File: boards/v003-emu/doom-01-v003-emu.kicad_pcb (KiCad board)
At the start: 2 copper layers, 96 x 50 mm, 36 parts, among them SW9 JS102011SAQN, U1 CH32V003F4P6, U2 APS6404L-3SQR-SN, U3 W25Q128JVSIQ, U4 TPS61023DRLR

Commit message: PCBKit's mark and pcbkit.io on every board; the RP2350 handheld ready to order
The handheld runs from two 18650 cells in parallel behind a DW01A protector and a reverse-cell
P-MOSFET, charged at up to 500 mA from the Pico's USB-C by a BQ24075 (power path into VSYS, timers
off for 6 Ah), with an on/off switch on 3V3_EN, M3 holes, ground pours and the console on pads.
Every assembled part has a JLCPCB code in stock (Basic where there is one); the module sockets are
in the BOM, the modules listed in the order's README. Check complete, the ready review clean.
Every board: routed and checked complete with the new mark.
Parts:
- added logo: , Logo_PCBKit_pcbkit.io, F.Cu at (122.0, 192.2)
- SW1, SW2, SW3, SW4, SW5, SW6, SW7, SW8: value (none) -> TS-1187A-B-A-B

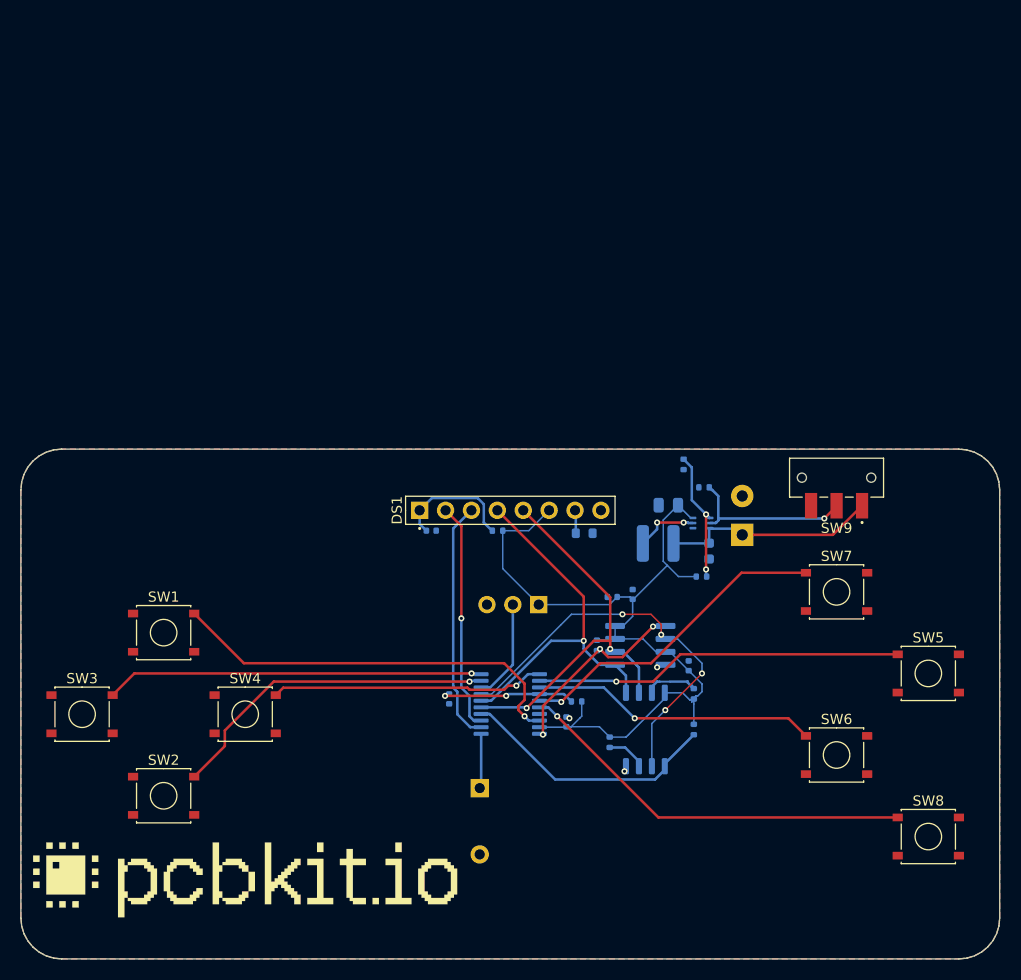
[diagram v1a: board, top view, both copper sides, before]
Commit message: v003-emu: two 18650 cells with protection, USB-C charging and an LDO; every part orderable
Two AA cells and a TPS61023 boost become two 18650 in parallel (Keystone 1042 holders on the
back) behind a reverse-cell P-FET and DW01A + FS8205A protection, a BQ24075 charger with power
path from a power-only USB-C port (750 mA PTC, TVS), and an AP2112K-3.3 LDO from SYS switched by
its enable (a boost cannot make 3.3 V from a cell above it). WCH-LinkE header J2 at the edge
(the ready lens now knows single-wire SWIO), the LCD's own decoupling, test pads, M3 holes; every
assembled part pinned to an LCSC code; the README says how to charge and flash.
check: complete, 0 errors, 0 warnings; ready lens: nothing to fix; fab export without --force.

Claude-Session: https://claude.ai/code/session_01ATmMmxyrWxFwR3nTdXUrcx
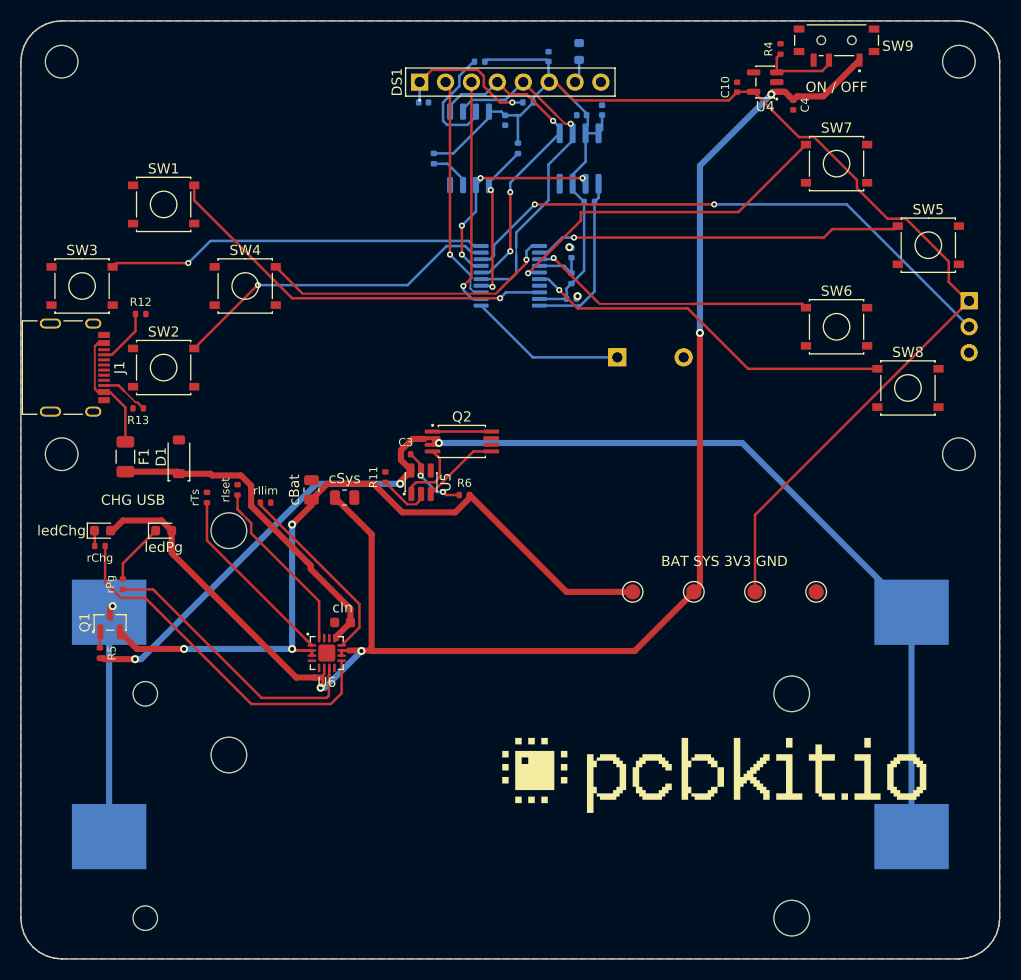
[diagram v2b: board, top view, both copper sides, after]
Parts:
- removed L1: 1uH, L_Power_4x4mm
- added BT2: 1042, BatteryHolder_Keystone_1042_1x18650, B.Cu at (148.0, 166.0)
- added C10: 1uF, C_0402_1005Metric, F.Cu at (170.2, 114.5)
- added C9: 100nF, C_0402_1005Metric, B.Cu at (151.8, 111.5)
- added D1: tvs 5V, D_SOD-123, F.Cu at (115.5, 150.8)
- added F1: PTC 680mA, Fuse_1206_3216Metric, F.Cu at (110.2, 150.8)
- added H1: , MountingHole_3.2mm_M3, F.Cu at (104.0, 150.5)
- added H2: , MountingHole_3.2mm_M3, F.Cu at (192.0, 150.5)
- added H3: , MountingHole_3.2mm_M3, F.Cu at (104.0, 112.0)
- added H4: , MountingHole_3.2mm_M3, F.Cu at (192.0, 112.0)
- added J1: , USB_C_Receptacle_USB2.0_16P, F.Cu at (108.2, 142.0)
- added Q1: AO3401A, SOT-23, F.Cu at (108.8, 167.0)
- added Q2: FS8205A, TSSOP-8_4.4x2.93mm_P0.65mm, F.Cu at (143.2, 149.2)
- added R11: 1kohm, R_0402_1005Metric, F.Cu at (135.8, 152.8)
- added R12: 5.1kohm, R_0402_1005Metric, F.Cu at (111.8, 136.8)
- added R13: 5.1kohm, R_0402_1005Metric, F.Cu at (111.5, 146.0)
- added U5: DW01A, SOT-6_1.6x2.9mm_P0.95mm, F.Cu at (139.2, 153.2)
- added U6: BQ24075RGTR, QFN-16-1EP_3x3mm_P0.5mm_EP1.68x1.68mm, F.Cu at (130.0, 170.0)
- added cBat: 4.7uF, C_0805_2012Metric, F.Cu at (128.5, 154.0)
- added cIn: 1uF, C_0603_1608Metric, F.Cu at (131.6, 167.0)
- added cSys: 4.7uF, C_0805_2012Metric, F.Cu at (131.8, 154.8)
- added ledChg: red, LED_0603_1608Metric, F.Cu at (108.0, 158.0)
- added ledPg: green, LED_0603_1608Metric, F.Cu at (114.0, 158.0)
- added rChg: 1.5kohm, R_0402_1005Metric, F.Cu at (107.8, 159.5)
- added rIlim: 1.18kohm, R_0402_1005Metric, F.Cu at (124.0, 155.2)
- added rIset: 1.13kohm, R_0402_1005Metric, F.Cu at (121.2, 154.0)
- added rPg: 1.5kohm, R_0402_1005Metric, F.Cu at (110.0, 163.2)
- added rTs: 10kohm, R_0402_1005Metric, F.Cu at (118.2, 154.8)
- added tpBat: , TestPoint_Round_D1.5mm, F.Cu at (160.0, 164.0)
- added tpGnd: , TestPoint_Round_D1.5mm, F.Cu at (178.0, 164.0)
- added tpSys: , TestPoint_Round_D1.5mm, F.Cu at (166.0, 164.0)
- added tpV3: , TestPoint_Round_D1.5mm, F.Cu at (172.0, 164.0)
- BT1: value 2xAA battery holder with leads -> 1042; footprint BatteryLeads_2x_D1.1mm_P3.81mm -> BatteryHolder_Keystone_1042_1x18650
- C3: value 10uF -> 100nF; footprint C_0603_1608Metric -> C_0402_1005Metric; moved to F.Cu
- C4: value 22uF -> 1uF; footprint C_0805_2012Metric -> C_0402_1005Metric; moved to F.Cu
- R4: moved to F.Cu
- R5: value 453kohm -> 100kohm; moved to F.Cu
- R6: value 100kohm -> 100ohm; moved to F.Cu
- SW9: value JS102011SAQN -> MSK12C02; footprint SW_Slide_SPDT_CK_JS102011SAQN_Horizontal -> SW_Slide_SPDT_Shouhan_MSK12C02
- U4: value TPS61023DRLR -> AP2112K-3.3TRG1; footprint SOT-563 -> SOT-23-5; moved to F.Cu
- moved R10 65.5 mm to (145.0, 112.0), turned to 0 degrees
- moved R9 59.8 mm to (140.5, 121.5)
- moved R8 59.6 mm to (148.8, 120.5)
- moved U3 59.6 mm to (144.0, 120.5)
- moved R5 59.5 mm to (107.8, 170.0), turned to 270 degrees
- moved C8 56.4 mm to (147.5, 117.8), turned to 90 degrees
- moved J2 52.4 mm to (193.0, 138.0), turned to 0 degrees
- moved BZ1 48.5 mm to (161.8, 141.0), turned to 180 degrees
- moved U2 48.1 mm to (154.8, 121.5), turned to 270 degrees
- moved C7 47.8 mm to (157.0, 116.8), turned to 270 degrees
- moved C6 47.3 mm to (155.0, 117.2), turned to 0 degrees
- moved R3 47.3 mm to (154.8, 111.0), turned to 270 degrees
- moved logo 47.1 mm to (168.0, 182.0)
- moved C1 45.4 mm to (154.0, 130.8), turned to 270 degrees
- moved SW8 44.0 mm to (187.0, 144.0)
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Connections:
- BT1 pad 1: VBAT -> CELL_N
- BT1 pad 2: GND -> BAT_IN
- C3 pad 1: VBAT -> CELL_N
- C3 pad 2: GND -> Net-(C3-1)
- C4 pad 1: V3 -> SYS
- R4 pad 1: BOOST_EN -> LDO_EN
- R5 pad 1: V3 -> reversed/gate
- R5 pad 2: FB -> CELL_N
- R6 pad 1: FB -> Net-(C3-1)
- R6 pad 2: GND -> BAT
- SW9 pad 1: VBAT -> SYS
- SW9 pad 2: BOOST_EN -> LDO_EN
- SW9 pad 3: GND -> (no net)
- U4 pad 1: FB -> SYS
- U4 pad 2: BOOST_EN -> GND
- U4 pad 3: VBAT -> LDO_EN
- U4 pad 4: GND -> (no net)
- U4 pad 5: SW_NODE -> V3
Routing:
- net SYS: track 0.00 -> 152.3 mm, vias 0 -> 4
- net CELL_N: track 0.00 -> 119.0 mm, vias 0 -> 3
- net BAT: track 0.00 -> 73.6 mm, vias 0 -> 3
- net V3: track 91.4 -> 146.9 mm
- net SWIO: track 9.95 -> 55.6 mm, vias 0 -> 2
- net CHG_N: track 0.00 -> 35.3 mm
- net VBUS: track 0.00 -> 32.6 mm
- net PG_N: track 0.00 -> 27.5 mm
- net BAT_IN: track 0.00 -> 22.0 mm, vias 0 -> 1
- net VBAT: track 21.4 -> 0.00 mm
- net TS: track 0.00 -> 19.0 mm
- net ILIM: track 0.00 -> 18.7 mm
- net ISET: track 0.00 -> 17.3 mm
- net BOOST_EN: track 16.7 -> 0.00 mm, vias 1 -> 0
- net MISO: track 39.6 -> 25.7 mm
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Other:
- board size 96 x 50 mm -> 96 x 92 mm
- board text added: "+"
- board text added: "-"
- board text added: "2 x 18650 Li-ion 3.7 V"
- board text added: "3V3 SWIO GND"
- board text added: "BAT SYS 3V3 GND"
- board text added: "CHG USB"
- board text added: "ON / OFF"
